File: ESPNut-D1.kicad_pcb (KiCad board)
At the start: 2 copper layers, 46 parts, among them J1 USB_C_Receptacle_USB2.0, J2 ESP_CONN, J3 USB_PADS, J4 ESP_PROG, Q1 BC817, Q2 BC817, Q3 Si2302CDS, SW1 ESP_RST, SW2 ESP_BOOT, SW3 ESP_VDD_SW, SW4 POW_CTRL, U1 CH340G, U2 MIC5219-3.3YM5, Y1 12MHz

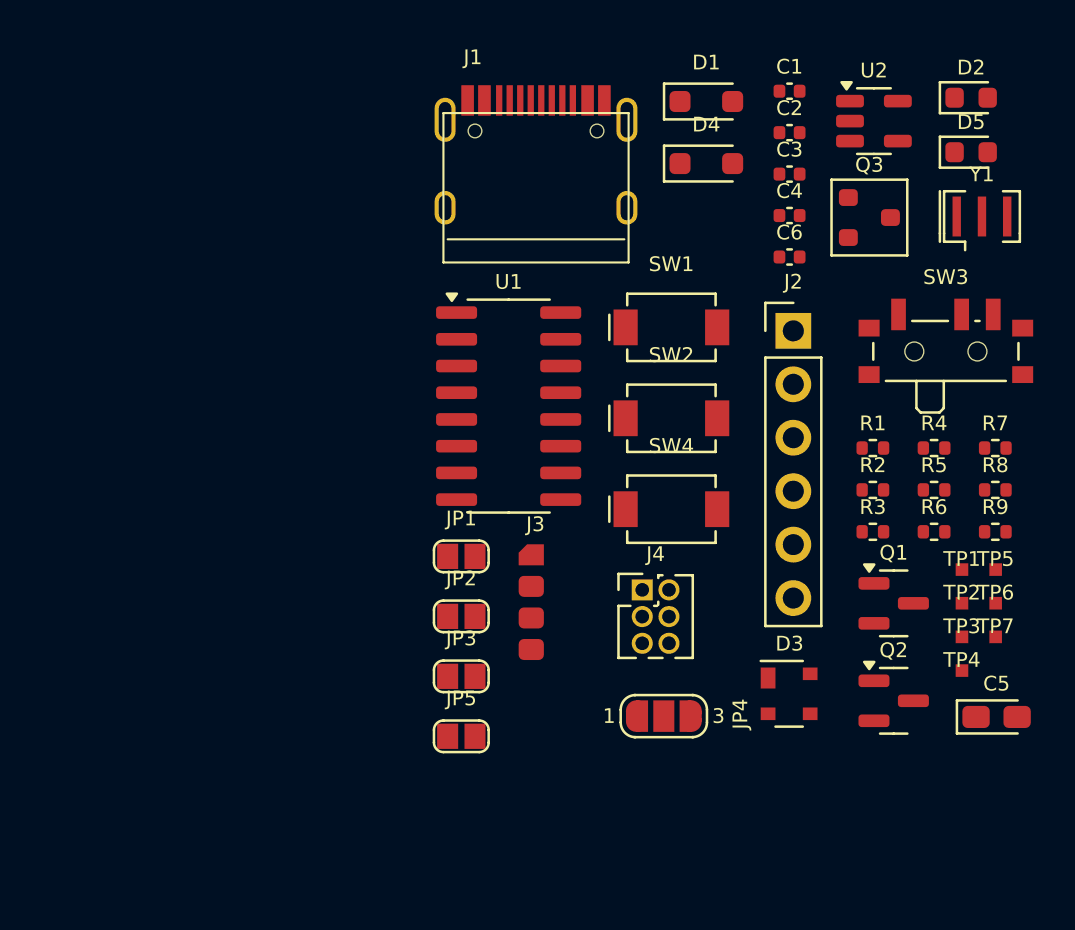
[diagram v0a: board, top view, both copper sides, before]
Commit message: Placement completed
- Added breakout pads for the LEDs.
- Changed USB-C connector footprint to SMD one.
- Added PCB outline.
- Placed all components.
- Added silkscreen labels and logos.
- Routing pending.
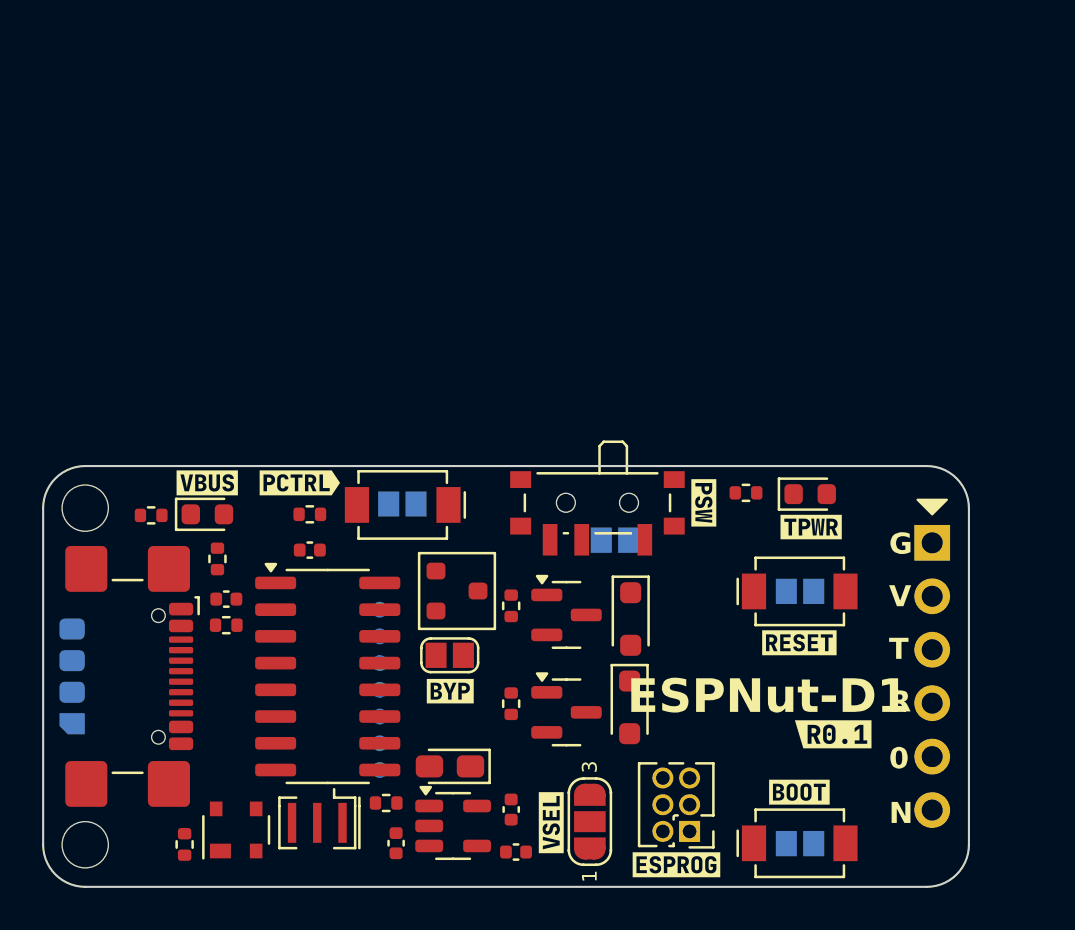
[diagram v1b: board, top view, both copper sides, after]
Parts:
- added G***: LOGO, CSE_Graphics:CSE-Logomark-20.4x5mm, B.Cu at (165.1, 126.8)
- added H1: MountingHole, MountingHole:MountingHole_2.2mm_M2_DIN965, F.Cu at (139.0, 118.0)
- added H2: MountingHole, MountingHole:MountingHole_2.2mm_M2_DIN965, F.Cu at (139.0, 134.0)
- added JP5: ESP_VDD_SW, CSE_Solder-Jumper:Solder-Jumper-1x2_P1.3mm_Open_Rounded_1.0x1.2mm, B.Cu at (164.2, 119.5)
- added TP10: CTS, SparkFun-Connector:TestPoint-0.75mm, B.Cu at (174.2, 117.3)
- added TP11: CTS, SparkFun-Connector:TestPoint-0.75mm, B.Cu at (172.6, 117.3)
- added TP8: CTS, SparkFun-Connector:TestPoint-0.75mm, B.Cu at (145.6, 118.3)
- added TP9: CTS, SparkFun-Connector:TestPoint-0.75mm, B.Cu at (144.0, 118.3)
- added kibuzzard-67F0B0FE: G***, kibuzzard-67F0B0FE, F.Cu at (168.4, 117.8)
- added kibuzzard-67F0B0FE: G***, kibuzzard-67F0B0FE, B.Cu at (164.2, 121.2)
- added kibuzzard-67F0B12D: G***, kibuzzard-67F0B12D, F.Cu at (156.3, 126.7)
- added kibuzzard-67F0B13A: G***, kibuzzard-67F0B13A, F.Cu at (161.2, 132.9)
- added kibuzzard-67F0B154: G***, kibuzzard-67F0B154, F.Cu at (172.9, 131.5)
- added kibuzzard-67F0B154: G***, kibuzzard-67F0B154, B.Cu at (173.0, 132.3)
- added kibuzzard-67F0B15A: G***, kibuzzard-67F0B15A, F.Cu at (172.9, 124.4)
- added kibuzzard-67F0B15A: G***, kibuzzard-67F0B15A, B.Cu at (173.0, 123.6)
- added kibuzzard-67F0B186: G***, kibuzzard-67F0B186, F.Cu at (173.5, 118.9)
- added kibuzzard-67F0B186: G***, kibuzzard-67F0B186, B.Cu at (173.4, 118.6)
- added kibuzzard-67F0B222: G***, kibuzzard-67F0B222, F.Cu at (144.8, 116.8)
- added kibuzzard-67F0B222: G***, kibuzzard-67F0B222, B.Cu at (144.8, 119.7)
- added kibuzzard-67F0B314: G***, kibuzzard-67F0B314, F.Cu at (149.2, 116.8)
- added kibuzzard-67F0B829: G***, kibuzzard-67F0B829, F.Cu at (167.1, 134.9)
- added kibuzzard-67F0B847: G***, kibuzzard-67F0B847, F.Cu at (174.6, 128.8)
- added kibuzzard-67F0B847: G***, kibuzzard-67F0B847, B.Cu at (143.6, 134.3)
- added kibuzzard-67F0C2BD: G***, kibuzzard-67F0C2BD, B.Cu at (154.1, 119.5)
- added kibuzzard-67F0C2E8: G***, kibuzzard-67F0C2E8, B.Cu at (140.8, 123.8)
- added kibuzzard-67F0C300: G***, kibuzzard-67F0C300, B.Cu at (140.1, 125.2)
- added kibuzzard-67F0C30C: G***, kibuzzard-67F0C30C, B.Cu at (140.1, 126.8)
- added kibuzzard-67F0C318: G***, kibuzzard-67F0C318, B.Cu at (140.5, 128.2)
- J1: footprint CIRCUITSTATE_Connector_USB:Korean-Hroparts-Elec_TYPE-C-31-M-12 -> CSE_Connector_USB:USB_C_Receptacle_GCT_USB4110
- J3: footprint CIRCUITSTATE_Solderpads:Solderpad_1x4_Rectangular_Rounded_1.2x1mm_P1.5mm -> CSE_Solderpads:Solderpad_1x4_Rectangular_Rounded_1.2x1mm_P1.5mm; moved to B.Cu
- JP1, JP2: footprint CIRCUITSTATE_Solder-Jumper:SolderJumper-2_P1.3mm_Open_RoundedPad1.0x1.2mm -> CSE_Solder-Jumper:Solder-Jumper-1x2_P1.3mm_Open_Rounded_1.0x1.2mm; moved to B.Cu
- JP3: footprint CIRCUITSTATE_Solder-Jumper:SolderJumper-2_P1.3mm_Open_RoundedPad1.0x1.2mm -> CSE_Solder-Jumper:Solder-Jumper-1x2_P1.3mm_Open_Rounded_1.0x1.2mm
- JP4: footprint CIRCUITSTATE_Solder-Jumper:SolderJumper-3_P1.3mm_Open_RoundedPad1.0x1.5mm_NumberLabels -> CSE_Solder-Jumper:Solder-Jumper-1x3_P1.3mm_Open_Rounded_1.0x1.5mm_Labels
- JP6: renamed from JP5; footprint CIRCUITSTATE_Solder-Jumper:SolderJumper-2_P1.3mm_Open_RoundedPad1.0x1.2mm -> CSE_Solder-Jumper:Solder-Jumper-1x2_P1.3mm_Open_Rounded_1.0x1.2mm; moved to B.Cu
- SW1, SW2, SW4: footprint CIRCUITSTATE_Switch_SMD:CK_SW_SPST_UK-B0273-SP25Y -> CSE_Switch_SMD:CK_SW_SPST_UK-B0273-SP25Y
- TP1, TP2, TP3, TP4, TP5, TP6, TP7: footprint CIRCUITSTATE_Solderpads:Solder-Pad_Rectangular_W0.6mm -> SparkFun-Connector:TestPoint-0.75mm; moved to B.Cu
- moved Y1 42.8 mm to (150.0, 133.0), turned to 180 degrees
- moved D2 41.3 mm to (144.8, 118.3)
- moved U2 39.0 mm to (156.5, 133.1)
- moved C3 36.9 mm to (153.8, 133.9), turned to 90 degrees
- moved C1 36.0 mm to (145.7, 122.3), turned to 180 degrees
- moved R3 35.9 mm to (143.7, 134.0), turned to -90 degrees
- moved R1 34.4 mm to (142.1, 118.3)
- moved R6 33.9 mm to (145.7, 123.6), turned to 180 degrees
- moved C4 32.9 mm to (159.5, 134.3)
- moved R8 32.6 mm to (149.7, 118.3)
- moved R2 31.3 mm to (145.3, 120.4), turned to 90 degrees
- moved J1 30.3 mm to (139.9, 126.0), turned to -90 degrees
- moved C2 30.2 mm to (149.7, 120.0), turned to 180 degrees
- moved R5 30.0 mm to (153.3, 132.0), turned to 180 degrees
- moved TP5 29.8 mm to (153.0, 126.6), turned to 180 degrees
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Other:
- board outline added: 44 x 20 mm
- board text added: "0"
- board text added: "ESPNut-D1"
- board text added: "G"
- board text added: "N"
- board text added: "R"
- board text added: "T"
- board text added: "V"
- board text added: "www.circuitstate.com"

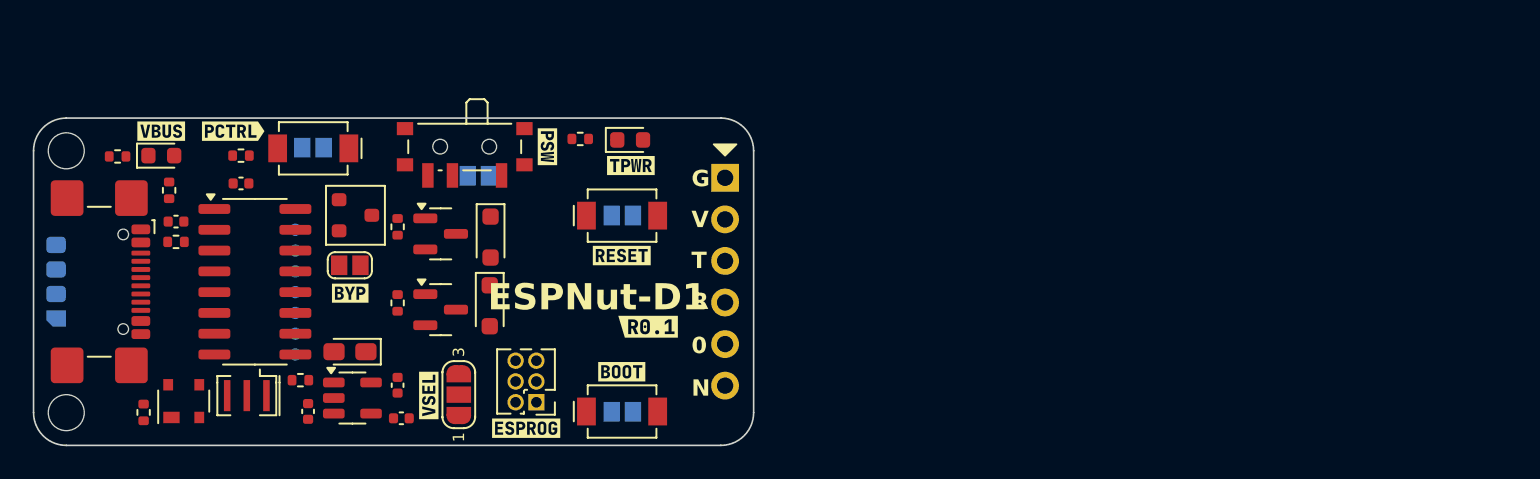
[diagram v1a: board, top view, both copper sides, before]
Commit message: Routing completed
- Added GND zones.
- DRC passes.
- Added more silkscreen labels.
- Added CIRCUITSTATE logo on the back silkscreen.
- Updated Fab layers.
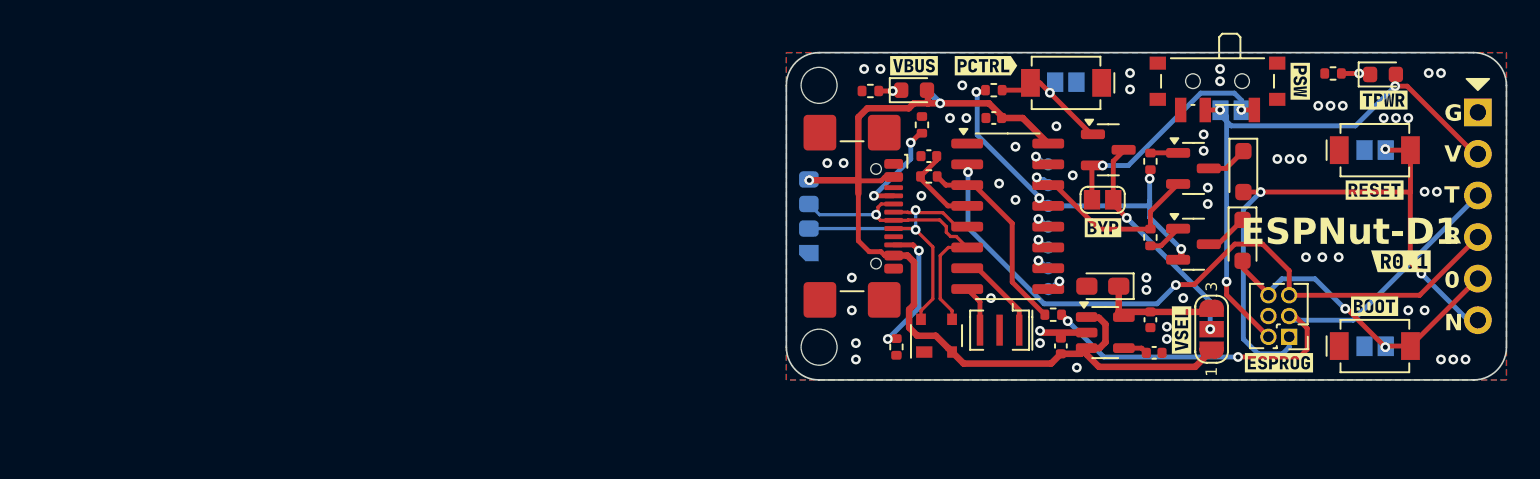
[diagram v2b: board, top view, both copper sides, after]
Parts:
- Q3: footprint Package_TO_SOT_SMD_AKL:SOT-23 -> Package_TO_SOT_SMD:SOT-23
- moved kibuzzard-67F0B847 46.4 mm to (189.8, 130.5)
- moved C1 46.2 mm to (191.7, 118.3)
- moved C2 46.2 mm to (195.7, 116.0)
- moved C3 46.2 mm to (199.8, 129.9)
- moved C4 46.2 mm to (205.5, 130.3)
- moved C5 46.2 mm to (202.3, 126.3)
- moved C6 46.2 mm to (205.2, 128.3)
- moved D1 46.2 mm to (210.9, 119.3)
- moved D2 46.2 mm to (190.8, 114.3)
- moved D3 46.2 mm to (192.2, 129.3)
- moved D4 46.2 mm to (210.9, 123.5)
- moved D5 46.2 mm to (219.5, 113.3)
- moved G*** 46.2 mm to (211.1, 122.8)
- moved H1 46.2 mm to (185.0, 114.0)
- moved H2 46.2 mm to (185.0, 130.0)
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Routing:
- net VBUS: track 0.00 -> 61.7 mm, vias 0 -> 2
- net /ESP_RX0: track 0.00 -> 42.1 mm, vias 0 -> 2
- net /ESP_NRST: track 0.00 -> 37.6 mm, vias 0 -> 3
- net /ESP_VDD_O: track 0.00 -> 36.5 mm, vias 0 -> 3
- net /ESP_TX0: track 0.00 -> 33.8 mm, vias 0 -> 2
- net /DTR: track 0.00 -> 22.3 mm, vias 0 -> 4
- net /USB_D+: track 0.00 -> 20.2 mm, vias 0 -> 2
- net /ESP_IO0: track 0.00 -> 19.5 mm, vias 0 -> 2
- net /USB_D-: track 0.00 -> 18.5 mm, vias 0 -> 1
- net Net-(JP3-A): track 0.00 -> 14.7 mm, vias 0 -> 2
- net /ESP_VDD_I: track 0.00 -> 13.7 mm, vias 0 -> 2
- net /RTS: track 0.00 -> 12.7 mm, vias 0 -> 1
- net Net-(U1-RXD): track 0.00 -> 12.2 mm
- net Net-(J1-CC2): track 0.00 -> 8.41 mm, vias 0 -> 2
- net +3V3: track 0.00 -> 7.79 mm
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- added copper zone on B.Cu, net GND
- added copper zone on F.Cu, net GND
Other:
- board text added: "R232"
- board text added: "~CTS"
- board text added: "~DCD"
- board text added: "~DSR"
- board text added: "~DTR"
- board text added: "~RI"
- board text added: "~RTS"

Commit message: Updated BoM
- Updated BoM.
  - Assigned all MPNs.
  - Changed the 10 uF, 0402 capacitor to 4.7 uF, 0402.
- Imported all changes to the PCB.
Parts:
- C3, C6: value 10uF -> 4.7uF
- H1, H2: value MountingHole -> Mounting Hole

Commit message: Generated manufacturing files
- Added KiExport configuration and script.
- Added dimension drawings.
- Added board characteristics and stackup table.
- Added `OSHW` logo.
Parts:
- added G***: LOGO, LOGO, B.Cu at (140.2, 72.1)
- moved C1 76.6 mm to (127.7, 76.3)
- moved C2 76.6 mm to (131.7, 74.0)
- moved C3 76.6 mm to (135.8, 87.9)
- moved C4 76.6 mm to (141.5, 88.3)
- moved C5 76.6 mm to (138.3, 84.3)
- moved D1 76.6 mm to (146.9, 77.3)
- moved D2 76.6 mm to (126.8, 72.3)
- moved D4 76.6 mm to (146.9, 81.5)
- moved D5 76.6 mm to (155.5, 71.3)
- moved G*** 76.6 mm to (147.1, 80.8)
- moved H1 76.6 mm to (121.0, 72.0)
- moved H2 76.6 mm to (121.0, 88.0)
- moved J1 76.6 mm to (121.9, 80.0)
- moved J2 76.6 mm to (161.3, 73.7)
- moved J3 76.6 mm to (120.4, 80.0)
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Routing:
- net GND: vias 55 -> 53
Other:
- board text added: "0 mm"
- board text added: "0.01 mm"
- board text added: "0.02"
- board text added: "0.035 mm"
- board text added: "0.2000 mm"
- board text added: "0.2000 mm / 0.2000 mm"
- board text added: "1"
- board text added: "1.51 mm"
- board text added: "1.6000 mm"
- board text added: "2"
- board text added: "3.3"
- board text added: "4.5"
- board text added: "44.0000 mm x 20.0000 mm"
- board text added: "B.Cu"
- board text added: "B.Mask"
- board text added: "B.Paste"
- board text added: "B.Silkscreen"
- board text added: "BOARD CHARACTERISTICS"
- board text added: "Board Thickness:"
- board text added: "Board overall dimensions:"
- board text added: "Bottom Silk Screen"
- board text added: "Bottom Solder Mask"
- board text added: "Bottom Solder Paste"
- board text added: "Castellated pads:"
- board text added: "Color"
- board text added: "Copper Finish:"
- board text added: "Copper Layer Count:"
- board text added: "Designed with KiCad"
- board text added: "Dielectric"
- board text added: "ENIG"
- board text added: "Edge card connectors:"
- board text added: "Epsilon R"
- board text added: "F.Cu"
- board text added: "F.Mask"
- board text added: "F.Paste"
- board text added: "F.Silkscreen"
- board text added: "FR4"
- board text added: "Impedance Control:"
- board text added: "Layer Name"
- board text added: "Loss Tangent"
- board text added: "Material"
- board text added: "Min hole diameter:"
- board text added: "Min track/spacing:"
- board text added: "No"
- board text added: "Not specified"
- board text added: "OSHW"
- board text added: "Plated Board Edge:"
- board text added: "Thickness (mm)"
- board text added: "Top Silk Screen"
- board text added: "Top Solder Mask"
- board text added: "Top Solder Paste"
- board text added: "Type"
- board text added: "copper"
- board text added: "core"

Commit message: Added fiducial
- Added fiducial to the front side.
- Generated new manufacturing files.
- Updated Readme.
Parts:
- added FD1: Fiducial_0.75mm_Mask1.5mm, Fiducial:Fiducial_0.75mm_Mask1.5mm, F.Cu at (149.8, 75.1)
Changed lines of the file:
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@@
 	(title_block
 		(title "ESPNut-D1")
-		(date "2025-04-09")
+		(date "2025-04-23")
 		(rev "0.1")
 		(company "CIRCUITSTATE Electronics LLP")
@@
 		)
 		(embedded_fonts no)
+	)
+	(footprint "Fiducial:Fiducial_0.75mm_Mask1.5mm"
+		(locked yes)
+		(layer "F.Cu")
+		(at 149.8 75.1)
+		(descr "Circular Fiducial, 0.75mm bare copper, 1.5mm soldermask opening (Level B)")
+		(tags "fiducial")
+		(property "Reference" "FD1"
+			(at 0 -2 0)
+			(unlocked yes)
+			(layer "F.SilkS")
+			(hide yes)
+			(effects
+				(font
+					(size 0.7 0.7)
+					(thickness 0.15)
+				)
+			)
+		)
+		(property "Value" "Fiducial_0.75mm_Mask1.5mm"
+			(at 0.2 -1.1 0)
+			(unlocked yes)
+			(layer "F.Fab")
+			(effects
+				(font
+					(size 0.3 0.3)
+					(thickness 0.06)
+				)
+			)
+		)
+		(property "Datasheet" ""
+			(at 0 0 0)
+			(unlocked yes)
+			(layer "F.Fab")
+			(hide yes)
+			(effects
+				(font
+					(size 0.3 0.3)
+					(thickness 0.06)
+				)
+			)
+		)
+		(property "Description" ""
+			(at 0 0 0)
+			(unlocked yes)
+			(layer "F.Fab")
+			(hide yes)
+			(effects
+				(font
+					(size 0.3 0.3)
+					(thickness 0.06)
+				)
+			)
+		)
+		(attr smd board_only exclude_from_bom)
+		(fp_circle
+			(center 0 0)
+			(end 1 0)
+			(stroke
+				(width 0.05)
+				(type solid)
+			)
+			(fill no)
+			(layer "F.CrtYd")
+		)
+		(fp_circle
+			(center 0 0)
+			(end 0.75 0)
+			(stroke
+				(width 0.1)
+				(type solid)
+			)
+			(fill no)
+			(layer "F.Fab")
+		)
+		(fp_text user "${REFERENCE}"
+			(at 0 0 0)
+			(unlocked yes)
+			(layer "F.Fab")
+			(effects
+				(font
+					(size 0.3 0.3)
+					(thickness 0.06)
+				)
+			)
+		)
+		(pad "" smd circle
+			(at 0 0)
+			(size 0.75 0.75)
+			(layers "F.Cu" "F.Mask")
+			(solder_mask_margin 0.375)
+			(clearance 0.375)
+		)
+		(embedded_fonts no)
